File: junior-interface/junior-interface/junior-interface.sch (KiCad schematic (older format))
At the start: 19 parts, among them IC13 7427, IC14 74LS01, IC15 74LS30, IC16 74LS00, IC17 GAL16V8, IC2 2114, IC3 2114, IC4 2716, IC5 2716, J1 Conn_01x03_Male

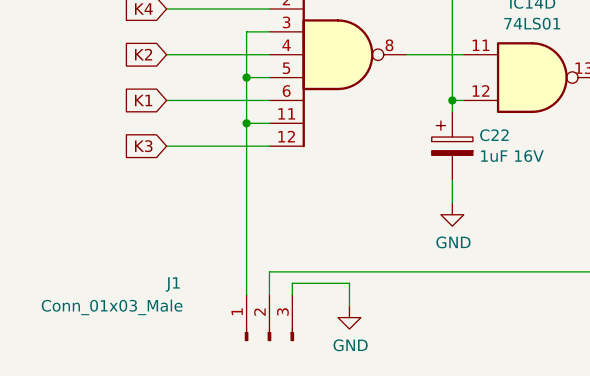
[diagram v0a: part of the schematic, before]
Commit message: junior interface schema
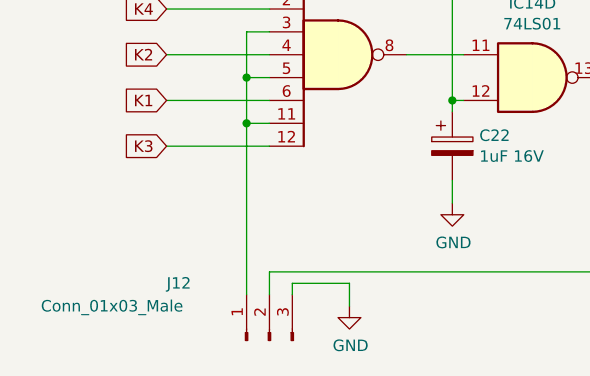
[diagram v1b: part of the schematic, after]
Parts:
- renumbered J1 to J12
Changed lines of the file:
@@
 	3950 6500 4050 6500
 $Comp
-L Connector:Conn_01x03_Male J1
+L Connector:Conn_01x03_Male J12
 U 1 1 5FD8F3EF
 P 1900 7450
-F 0 "J1" V 2150 7900 50  0000 R CNN
+F 0 "J12" V 2150 7900 50  0000 R CNN
 F 1 "Conn_01x03_Male" V 2050 8450 50  0000 R CNN
 F 2 "Pin_Headers:Pin_Header_Straight_1x03_Pitch2.54mm" H 1900 7450 50  0001 C CNN
@@
 Wire Wire Line
 	2250 7200 2250 7300
+Text Label 10050 850  0    50   ~ 0
+AB[0..15]
+Text Label 10050 1150 0    50   ~ 0
+DB[0..7]
 Wire Bus Line
 	8050 850  8050 3700
@@
 Wire Bus Line
 	800  850  8050 850
-Text Label 10050 850  0    50   ~ 0
-AB[0..15]
-Text Label 10050 1150 0    50   ~ 0
-DB[0..7]
 $EndSCHEMATC

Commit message: junior interface routage
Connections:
- net ABO is gone; now on net AB0: IC5.8 (A0)
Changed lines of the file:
@@
 DB7
 Text Label 3450 1450 1    50   ~ 0
-ABO
+AB0
 Text Label 3100 1450 1    50   ~ 0
 AB10

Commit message: junior interface routage
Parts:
- removed IC13: 7427, elektor:DIL-14, symbol 74xx_IEEE:7427
- removed unit 5 of IC16
- added IC13: 74LS27, symbol 74xx:74LS27
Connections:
- net AB13: now also IC13.5
- net AB14: now also IC13.4
- net AB15: now also IC13.3
- net EX: now also IC13.8
- net GND: now also IC13.10, IC13.9
- new net: IC13.11, IC13.6
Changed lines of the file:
@@
-$EndComp
-$Comp
-L 74xx_IEEE:7427 IC13
-U 2 1 5F9376A0
-P 8850 3450
-F 0 "IC13" H 8850 3866 50  0000 C CNN
-F 1 "7427" H 8850 3775 50  0000 C CNN
-F 2 "elektor:DIL-14" H 8850 3450 50  0001 C CNN
-F 3 "" H 8850 3450 50  0001 C CNN
-	2    8850 3450
-	1    0    0    -1
 $EndComp
 $Comp
@@
 	2550 4300 2600 4300
 $Comp
-L 74xx:74LS00 IC16
-U 5 1 5FBBFF19
-P 1650 4200
-F 0 "IC16" H 1650 4525 50  0000 C CNN
-F 1 "74LS00" H 1650 4434 50  0000 C CNN
-F 2 "elektor:DIL-14" H 1650 4200 50  0001 C CNN
-F 3 "http://www.ti.com/lit/gpn/sn74ls00" H 1650 4200 50  0001 C CNN
-	5    1650 4200
-	1    0    0    -1
-$EndComp
-$Comp
-L power:+5V #PWR0130
-U 1 1 5FBCAC8D
-P 1650 3600
-F 0 "#PWR0130" H 1650 3450 50  0001 C CNN
-F 1 "+5V" H 1665 3773 50  0000 C CNN
-F 2 "" H 1650 3600 50  0001 C CNN
-F 3 "" H 1650 3600 50  0001 C CNN
-	1    1650 3600
-	1    0    0    -1
-$EndComp
-$Comp
-L power:GND #PWR0131
-U 1 1 5FBCAF08
-P 1650 4800
-F 0 "#PWR0131" H 1650 4550 50  0001 C CNN
-F 1 "GND" H 1655 4627 50  0000 C CNN
-F 2 "" H 1650 4800 50  0001 C CNN
-F 3 "" H 1650 4800 50  0001 C CNN
-	1    1650 4800
-	1    0    0    -1
-$EndComp
-Wire Wire Line
-	1650 3600 1650 3700
-Wire Wire Line
-	1650 4700 1650 4800
-$Comp
-L 74xx_IEEE:7427 IC13
-U 3 1 5FBDF24B
-P 10000 3600
-F 0 "IC13" H 10000 4016 50  0000 C CNN
-F 1 "7427" H 10000 3925 50  0000 C CNN
-F 2 "elektor:DIL-14" H 10000 3600 50  0001 C CNN
-F 3 "" H 10000 3600 50  0001 C CNN
-	3    10000 3600
-	1    0    0    1
-$EndComp
-$Comp
 L power:GND #PWR0132
 U 1 1 5FBDF64E
-P 9400 3950
-F 0 "#PWR0132" H 9400 3700 50  0001 C CNN
-F 1 "GND" H 9405 3777 50  0000 C CNN
-F 2 "" H 9400 3950 50  0001 C CNN
-F 3 "" H 9400 3950 50  0001 C CNN
-	1    9400 3950
-	1    0    0    -1
-$EndComp
-Wire Wire Line
-	9500 3600 9400 3600
-Wire Wire Line
-	9400 3600 9400 3750
-Wire Wire Line
-	9500 3750 9400 3750
-Connection ~ 9400 3750
-Wire Wire Line
-	9400 3750 9400 3950
-Wire Wire Line
-	9350 3450 9500 3450
+P 9500 3900
+F 0 "#PWR0132" H 9500 3650 50  0001 C CNN
+F 1 "GND" H 9505 3727 50  0000 C CNN
+F 2 "" H 9500 3900 50  0001 C CNN
+F 3 "" H 9500 3900 50  0001 C CNN
+	1    9500 3900
+	1    0    0    -1
+$EndComp
+Wire Wire Line
+	9600 3550 9500 3550
+Wire Wire Line
+	9500 3550 9500 3650
 Connection ~ 8050 850
 Entry Wire Line
-	8050 3200 8150 3300
+	8050 3250 8150 3350
 Entry Wire Line
 	8050 3350 8150 3450
 Entry Wire Line
-	8050 3500 8150 3600
-Wire Wire Line
-	8350 3300 8150 3300
-Wire Wire Line
-	8150 3450 8350 3450
-Wire Wire Line
-	8150 3600 8350 3600
-Text Label 8200 3300 0    50   ~ 0
+	8050 3450 8150 3550
+Text Label 8200 3350 0    50   ~ 0
 AB15
 Text Label 8200 3450 0    50   ~ 0
 AB14
-Text Label 8200 3600 0    50   ~ 0
+Text Label 8200 3550 0    50   ~ 0
 AB13
-Text GLabel 10650 3600 2    50   Input ~ 0
+Text GLabel 10350 3550 2    50   Input ~ 0
 EX
 Wire Wire Line
-	10650 3600 10500 3600
+	10350 3550 10200 3550
 Text GLabel 1650 5900 0    50   Input ~ 0
 K5
@@
 Text Label 10050 1150 0    50   ~ 0
 DB[0..7]
+$Comp
+L 74xx:74LS27 IC13
+U 2 1 5F9B8CFD
+P 8800 3450
+F 0 "IC13" H 8800 3775 50  0000 C CNN
+F 1 "74LS27" H 8800 3684 50  0000 C CNN
+F 2 "" H 8800 3450 50  0001 C CNN
+F 3 "http://www.ti.com/lit/gpn/sn74LS27" H 8800 3450 50  0001 C CNN
+	2    8800 3450
+	1    0    0    -1
+$EndComp
+Wire Wire Line
+	8150 3350 8500 3350
+Wire Wire Line
+	8150 3450 8500 3450
+Wire Wire Line
+	8150 3550 8500 3550
+$Comp
+L 74xx:74LS27 IC13
+U 3 1 5F9DFDD4
+P 9900 3550
+F 0 "IC13" H 9900 3233 50  0000 C CNN
+F 1 "74LS27" H 9900 3324 50  0000 C CNN
+F 2 "" H 9900 3550 50  0001 C CNN
+F 3 "http://www.ti.com/lit/gpn/sn74LS27" H 9900 3550 50  0001 C CNN
+	3    9900 3550
+	1    0    0    1
+$EndComp
+Wire Wire Line
+	9600 3650 9500 3650
+Connection ~ 9500 3650
+Wire Wire Line
+	9500 3650 9500 3900
+Wire Wire Line
+	9100 3450 9600 3450
 Wire Bus Line
 	8050 850  8050 3700

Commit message: junior interface routage
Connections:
- net +5V: now also IC15.11, IC15.3, IC15.5, J12.1 (Pin_1)
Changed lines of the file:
@@
 Wire Wire Line
 	9100 3450 9600 3450
+$Comp
+L power:+5V #PWR0191
+U 1 1 5FA24972
+P 1800 5800
+F 0 "#PWR0191" H 1800 5650 50  0001 C CNN
+F 1 "+5V" H 1815 5973 50  0000 C CNN
+F 2 "" H 1800 5800 50  0001 C CNN
+F 3 "" H 1800 5800 50  0001 C CNN
+	1    1800 5800
+	1    0    0    -1
+$EndComp
+Wire Wire Line
+	1800 6100 1800 5800
 Wire Bus Line
 	8050 850  8050 3700
@@
 Wire Bus Line
 	800  850  8050 850
+Connection ~ 1800 6100
 $EndSCHEMATC

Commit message: junior interface routage
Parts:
- IC13: footprint (none) -> elektor:DIL-14
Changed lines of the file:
@@
 F 0 "IC13" H 8800 3775 50  0000 C CNN
 F 1 "74LS27" H 8800 3684 50  0000 C CNN
-F 2 "" H 8800 3450 50  0001 C CNN
+F 2 "elektor:DIL-14" H 8800 3450 50  0001 C CNN
 F 3 "http://www.ti.com/lit/gpn/sn74LS27" H 8800 3450 50  0001 C CNN
 	2    8800 3450
@@
 F 0 "IC13" H 9900 3233 50  0000 C CNN
 F 1 "74LS27" H 9900 3324 50  0000 C CNN
-F 2 "" H 9900 3550 50  0001 C CNN
+F 2 "elektor:DIL-14" H 9900 3550 50  0001 C CNN
 F 3 "http://www.ti.com/lit/gpn/sn74LS27" H 9900 3550 50  0001 C CNN
 	3    9900 3550
@@
 Wire Wire Line
 	1800 6100 1800 5800
+Connection ~ 1800 6100
 Wire Bus Line
 	8050 850  8050 3700
@@
 Wire Bus Line
 	800  850  8050 850
-Connection ~ 1800 6100
 $EndSCHEMATC

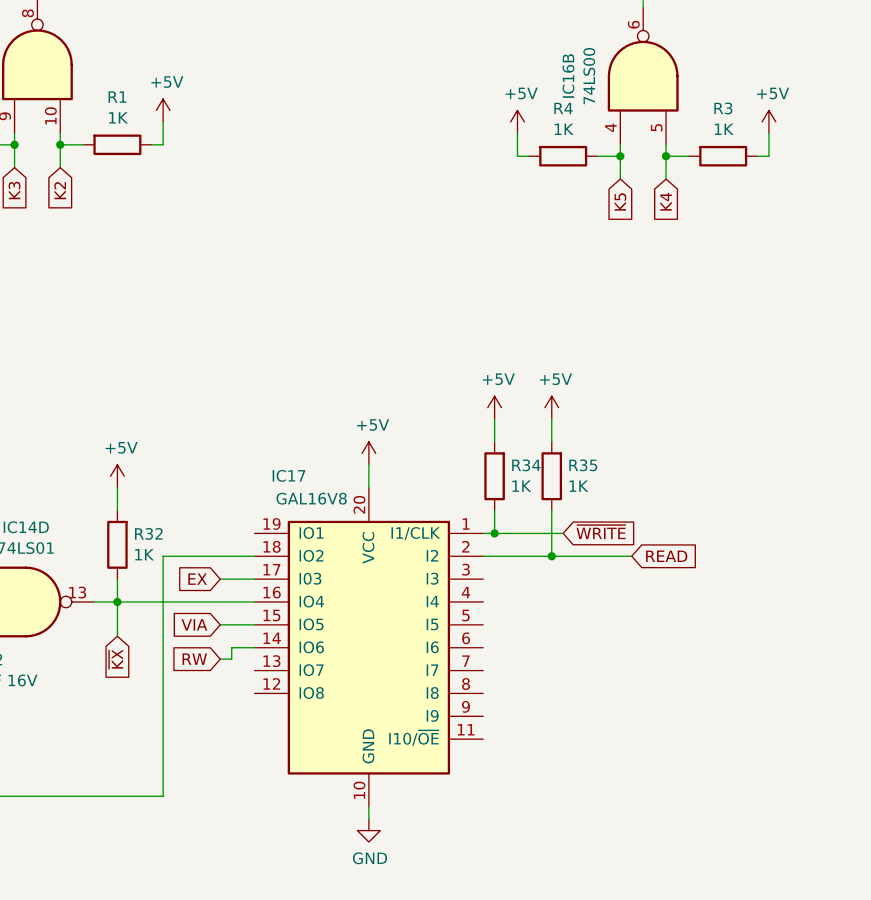
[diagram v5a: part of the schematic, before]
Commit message: junior interface routage complet
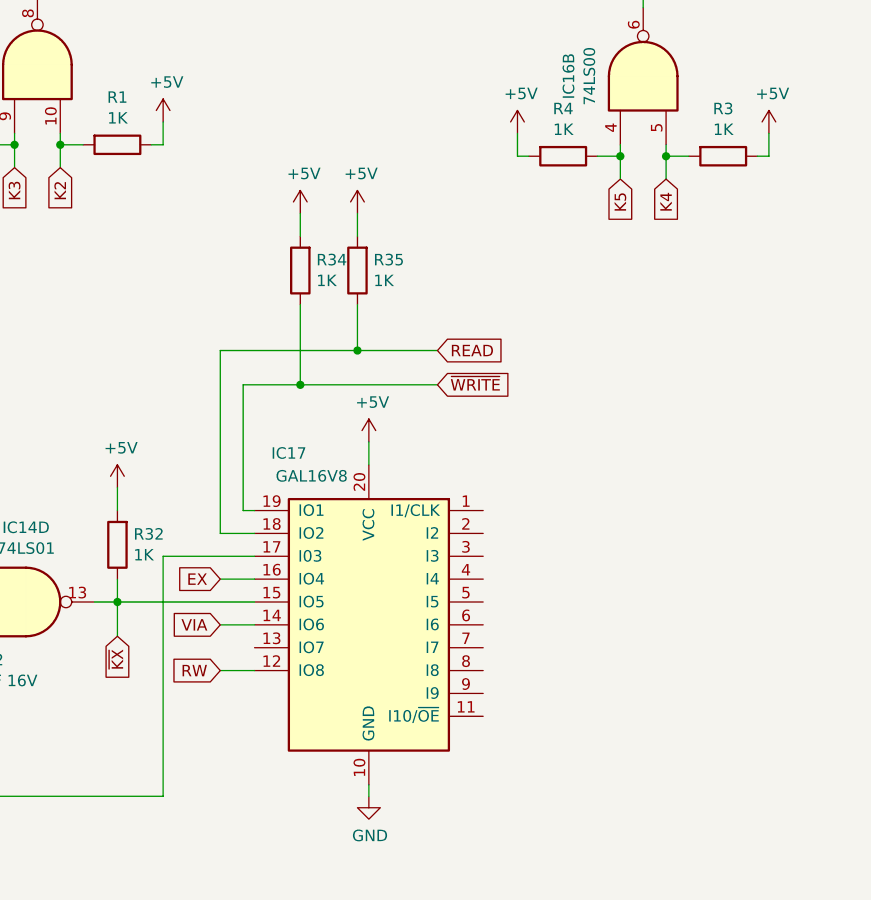
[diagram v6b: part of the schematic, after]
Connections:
- net EX: now also IC17.16 (IO4); no longer IC17.17 (I03)
- net READ: now also IC17.18 (IO2); no longer IC17.2 (I2)
- net RW: now also IC17.12 (IO8); no longer IC17.14 (IO6)
- net VIA: now also IC17.14 (IO6); no longer IC17.15 (IO5)
- net ~KX~: now also IC17.15 (IO5); no longer IC17.16 (IO4)
- net ~WRITE~: now also IC17.19 (IO1); no longer IC17.1 (I1/CLK)
- net at J12.2 (Pin_2): now also IC17.17 (I03); no longer IC17.18 (IO2)
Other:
- moved on the sheet: IC17, R34, R35
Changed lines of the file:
@@
 L Logic_Programmable:GAL16V8 IC17
 U 1 1 5F938ECD
-P 4550 6500
-F 0 "IC17" H 4900 7250 50  0000 C CNN
-F 1 "GAL16V8" H 4800 7150 50  0000 C CNN
-F 2 "elektor:DIL-20" H 4550 6500 50  0001 C CNN
-F 3 "" H 4550 6500 50  0001 C CNN
-	1    4550 6500
+P 4550 6400
+F 0 "IC17" H 4900 7150 50  0000 C CNN
+F 1 "GAL16V8" H 4800 7050 50  0000 C CNN
+F 2 "elektor:DIL-20" H 4550 6400 50  0001 C CNN
+F 3 "" H 4550 6400 50  0001 C CNN
+	1    4550 6400
 	-1   0    0    -1
 $EndComp
@@
 Wire Wire Line
 	2700 6750 2700 6850
-Text GLabel 5700 6100 2    50   Input ~ 0
+Text GLabel 4850 5200 2    50   Input ~ 0
 READ
-Text GLabel 5400 6000 2    50   Input ~ 0
+Text GLabel 4850 5350 2    50   Input ~ 0
 ~WRITE~
 Wire Wire Line
-	5700 6100 5350 6100
-Wire Wire Line
-	5050 6000 5100 6000
+	4850 5200 4500 5200
 Wire Wire Line
 	3450 6300 3450 6200
@@
 $EndComp
 Wire Wire Line
-	5100 5500 5100 5600
+	4250 4600 4250 4700
 $Comp
 L power:+5V #PWR0136
 U 1 1 5FD12BDA
-P 5100 5500
-F 0 "#PWR0136" H 5100 5350 50  0001 C CNN
-F 1 "+5V" H 5115 5673 50  0000 C CNN
-F 2 "" H 5100 5500 50  0001 C CNN
-F 3 "" H 5100 5500 50  0001 C CNN
-	1    5100 5500
+P 4250 4600
+F 0 "#PWR0136" H 4250 4450 50  0001 C CNN
+F 1 "+5V" H 4265 4773 50  0000 C CNN
+F 2 "" H 4250 4600 50  0001 C CNN
+F 3 "" H 4250 4600 50  0001 C CNN
+	1    4250 4600
 	1    0    0    -1
 $EndComp
@@
 L Device:R R34
 U 1 1 5FD12BE0
-P 5100 5750
-F 0 "R34" H 5030 5704 50  0000 R CNN
-F 1 "1K" H 5030 5795 50  0000 R CNN
-F 2 "elektor:Res-5" V 5030 5750 50  0001 C CNN
-F 3 "~" H 5100 5750 50  0001 C CNN
-	1    5100 5750
+P 4250 4850
+F 0 "R34" H 4180 4804 50  0000 R CNN
+F 1 "1K" H 4180 4895 50  0000 R CNN
+F 2 "elektor:Res-5" V 4180 4850 50  0001 C CNN
+F 3 "~" H 4250 4850 50  0001 C CNN
+	1    4250 4850
 	-1   0    0    1
 $EndComp
 Wire Wire Line
-	5350 5500 5350 5600
+	4500 4600 4500 4700
 $Comp
 L power:+5V #PWR0137
 U 1 1 5FD1D077
-P 5350 5500
-F 0 "#PWR0137" H 5350 5350 50  0001 C CNN
-F 1 "+5V" H 5365 5673 50  0000 C CNN
-F 2 "" H 5350 5500 50  0001 C CNN
-F 3 "" H 5350 5500 50  0001 C CNN
-	1    5350 5500
+P 4500 4600
+F 0 "#PWR0137" H 4500 4450 50  0001 C CNN
+F 1 "+5V" H 4515 4773 50  0000 C CNN
+F 2 "" H 4500 4600 50  0001 C CNN
+F 3 "" H 4500 4600 50  0001 C CNN
+	1    4500 4600
 	1    0    0    -1
 $EndComp
@@
 L Device:R R35
 U 1 1 5FD1D07D
-P 5350 5750
-F 0 "R35" H 5280 5704 50  0000 R CNN
-F 1 "1K" H 5280 5795 50  0000 R CNN
-F 2 "elektor:Res-5" V 5280 5750 50  0001 C CNN
-F 3 "~" H 5350 5750 50  0001 C CNN
-	1    5350 5750
+P 4500 4850
+F 0 "R35" H 4430 4804 50  0000 R CNN
+F 1 "1K" H 4430 4895 50  0000 R CNN
+F 2 "elektor:Res-5" V 4430 4850 50  0001 C CNN
+F 3 "~" H 4500 4850 50  0001 C CNN
+	1    4500 4850
 	-1   0    0    1
 $EndComp
-Wire Wire Line
-	5100 5900 5100 6000
-Connection ~ 5100 6000
-Wire Wire Line
-	5100 6000 5400 6000
-Wire Wire Line
-	5350 5900 5350 6100
-Connection ~ 5350 6100
-Wire Wire Line
-	5350 6100 5050 6100
 $Comp
 L power:GND #PWR0138
 U 1 1 5FD3D7B3
-P 4550 7250
-F 0 "#PWR0138" H 4550 7000 50  0001 C CNN
-F 1 "GND" H 4555 7077 50  0000 C CNN
-F 2 "" H 4550 7250 50  0001 C CNN
-F 3 "" H 4550 7250 50  0001 C CNN
-	1    4550 7250
+P 4550 7150
+F 0 "#PWR0138" H 4550 6900 50  0001 C CNN
+F 1 "GND" H 4555 6977 50  0000 C CNN
+F 2 "" H 4550 7150 50  0001 C CNN
+F 3 "" H 4550 7150 50  0001 C CNN
+	1    4550 7150
 	1    0    0    -1
 $EndComp
@@
 L power:+5V #PWR0139
 U 1 1 5FD3DC52
-P 4550 5700
-F 0 "#PWR0139" H 4550 5550 50  0001 C CNN
-F 1 "+5V" H 4565 5873 50  0000 C CNN
-F 2 "" H 4550 5700 50  0001 C CNN
-F 3 "" H 4550 5700 50  0001 C CNN
-	1    4550 5700
-	1    0    0    -1
-$EndComp
-Wire Wire Line
-	4550 5700 4550 5800
-Wire Wire Line
-	4550 7200 4550 7250
-Wire Wire Line
-	3450 6300 4050 6300
+P 4550 5600
+F 0 "#PWR0139" H 4550 5450 50  0001 C CNN
+F 1 "+5V" H 4565 5773 50  0000 C CNN
+F 2 "" H 4550 5600 50  0001 C CNN
+F 3 "" H 4550 5600 50  0001 C CNN
+	1    4550 5600
+	1    0    0    -1
+$EndComp
+Wire Wire Line
+	4550 5600 4550 5700
+Wire Wire Line
+	4550 7100 4550 7150
 Text GLabel 3900 6200 0    50   Input ~ 0
 EX
@@
 Wire Wire Line
 	3900 6400 4050 6400
-Text GLabel 3900 6550 0    50   Input ~ 0
+Text GLabel 3900 6600 0    50   Input ~ 0
 RW
-Wire Wire Line
-	3900 6550 3950 6550
-Wire Wire Line
-	3950 6550 3950 6500
-Wire Wire Line
-	3950 6500 4050 6500
 $Comp
 L Connector:Conn_01x03_Male J12
@@
 	1800 6100 1800 5800
 Connection ~ 1800 6100
+Wire Wire Line
+	4500 5000 4500 5200
+Wire Wire Line
+	4850 5350 4250 5350
+Wire Wire Line
+	4250 5000 4250 5350
+Wire Wire Line
+	4050 5900 4000 5900
+Wire Wire Line
+	4000 5900 4000 5350
+Wire Wire Line
+	4000 5350 4250 5350
+Connection ~ 4250 5350
+Wire Wire Line
+	4050 6000 3900 6000
+Wire Wire Line
+	3900 6000 3900 5200
+Wire Wire Line
+	3900 5200 4500 5200
+Connection ~ 4500 5200
+Wire Wire Line
+	3450 6300 4050 6300
+Wire Wire Line
+	3900 6600 4050 6600
 Wire Bus Line
 	8050 850  8050 3700
